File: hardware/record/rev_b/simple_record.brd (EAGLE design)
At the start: 34.9 x 30 mm, 20 parts, among them J1 PJ-035C, J2 SCREW-TERMINAL_2_0.100, J3 SCREW-TERMINAL_2_0.100, J4 SQUALL_HEADER, Q1 MOSFET-NCHANNELSMD, U1 MAX9923T

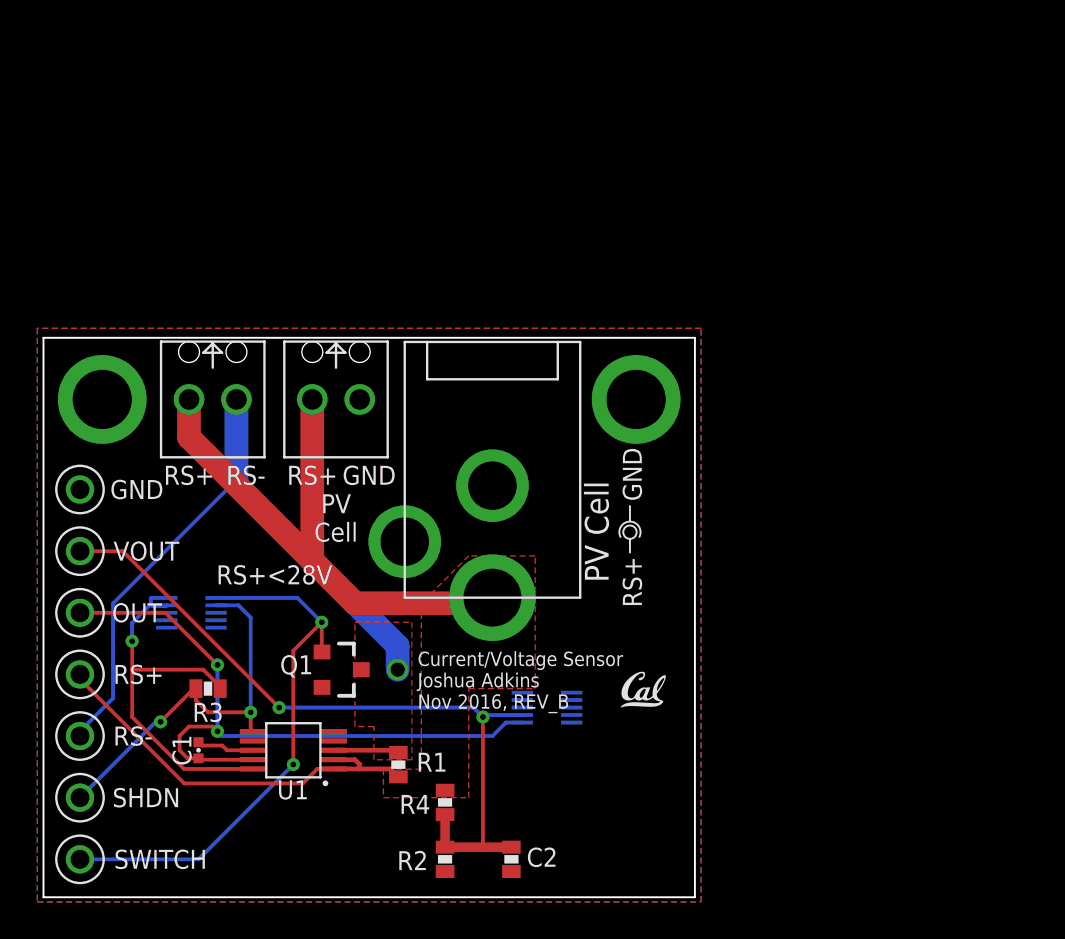
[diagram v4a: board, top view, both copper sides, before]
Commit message: updates
- added second barrel jack
- resized to be same size as logger board
- compressed test points to be 0.1" header friendly
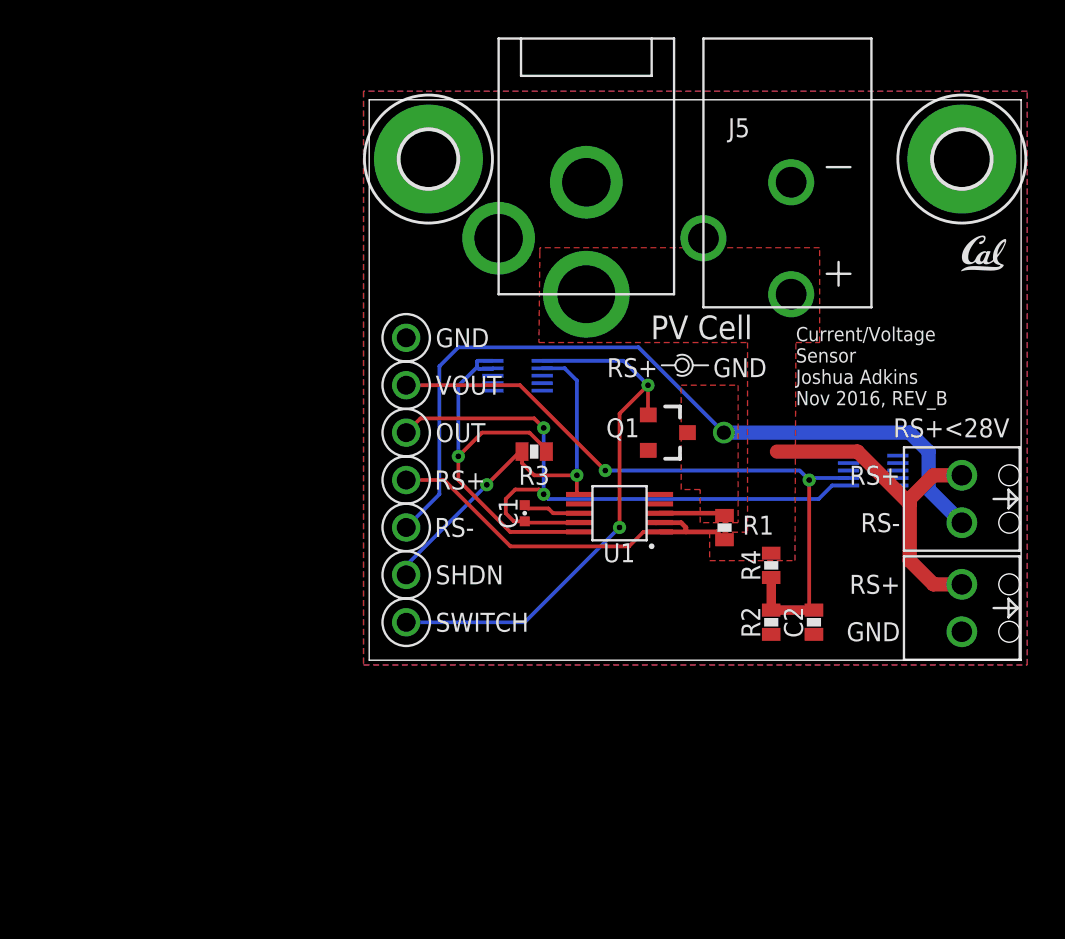
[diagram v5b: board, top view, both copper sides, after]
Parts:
- added H1, H2: MOUNT-PAD-ROUND3.0, holes:3,0-PAD
- added J5: PJ-102AH, connector:PJ-102AH
- moved J3 40.5 mm to (31.8, 8.64), turned to 90 degrees
- moved J2 35.3 mm to (31.8, 2.79), turned to 90 degrees
- moved U$1 29.6 mm to (31.7, 20.8)
- moved C1 21.6 mm to (8.33, 7.87)
- moved J4 21.6 mm to (17.5, 12.7)
- moved Q1 21.6 mm to (16.0, 12.2)
- moved R2 21.6 mm to (21.5, 2.03)
- moved R3 21.6 mm to (8.84, 11.2)
- moved R4 21.6 mm to (21.5, 5.08)
- moved TP3 21.6 mm to (1.98, 2.03)
- moved U1 21.6 mm to (13.4, 7.87)
- moved R1 21.6 mm to (19.0, 7.10)
- moved TP1 21.2 mm to (1.98, 4.57)
- moved TP6 20.7 mm to (1.98, 7.11)
- moved C2 20.6 mm to (23.8, 2.03)
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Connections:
- net GND: now also H1.B3,0, H2.B3,0, J5.2
- net PV+: now also J5.1
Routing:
- net PV+: track 53.1 -> 39.5 mm
- net IN-: track 38.8 -> 46.4 mm
- net VOUT: track 39.7 -> 37.0 mm
- net OUT: track 36.1 -> 35.4 mm
- net SHDN: track 20.7 -> 21.4 mm
- net VCC: track 21.4 -> 21.9 mm

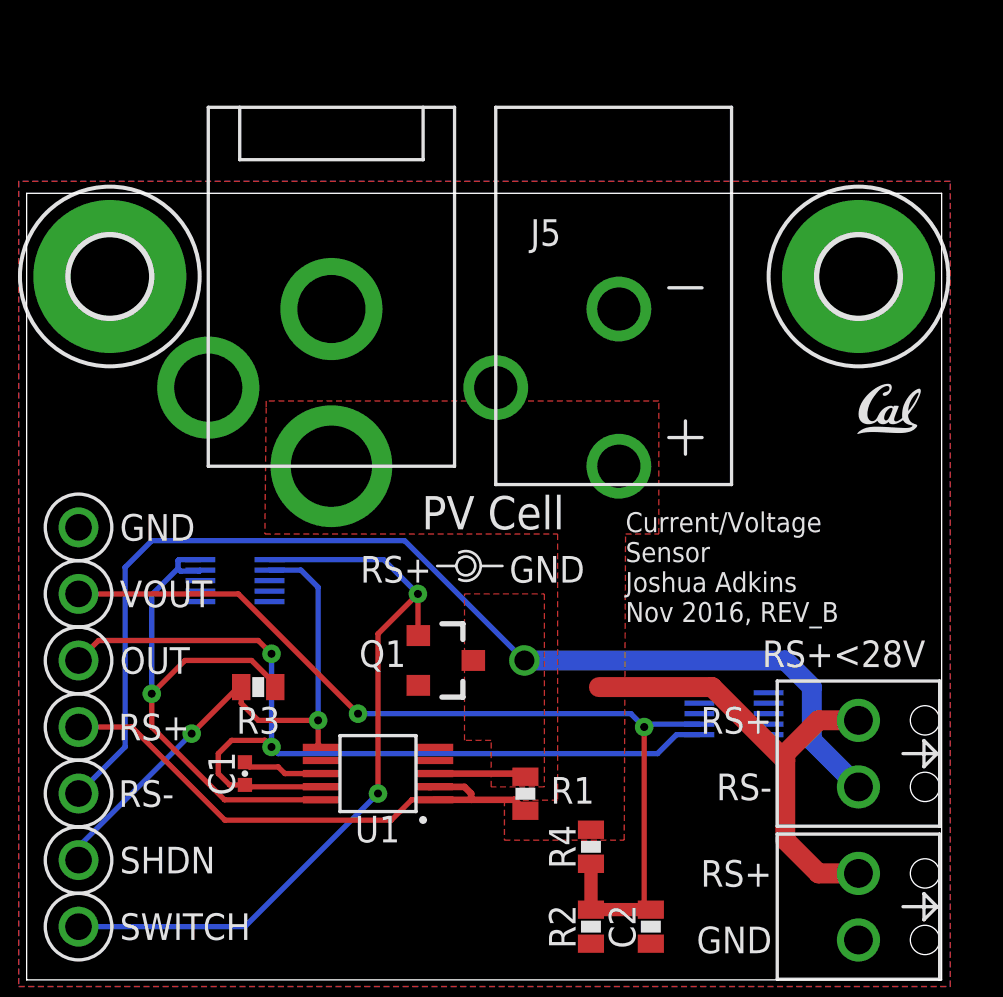
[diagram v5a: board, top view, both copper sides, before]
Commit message: better ground, moved barrel jacks farther out
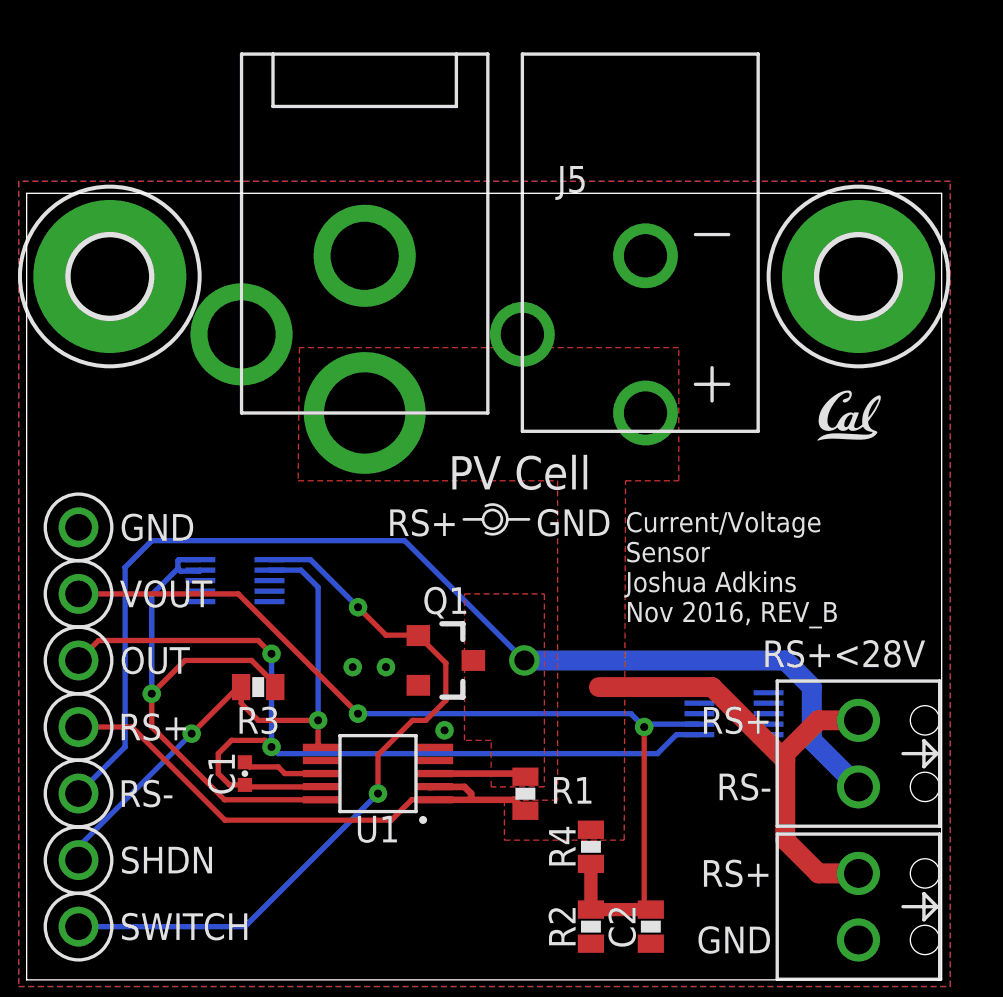
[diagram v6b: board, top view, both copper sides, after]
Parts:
- moved J1 2.40 mm to (12.9, 24.6)
- moved J5 2.27 mm to (23.6, 24.6)
- moved U$1 1.55 mm to (30.2, 20.6)
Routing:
- net CURRENT_SWITCH: track 29.6 -> 28.3 mm
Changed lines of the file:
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@@
 <setting verticaltext="up"/>
 </settings>
-<grid distance="10" unitdist="mil" unit="mil" style="lines" multiple="1" display="yes" altdistance="0.01" altunitdist="inch" altunit="inch"/>
+<grid distance="10" unitdist="mil" unit="mil" style="lines" multiple="1" display="yes" altdistance="1" altunitdist="mil" altunit="mil"/>
 <layers>
 <layer number="1" name="Top" color="4" fill="1" visible="yes" active="yes"/>
@@
 <text x="28.448" y="4.064" size="1.016" layer="25" font="vector" ratio="12" rot="R180" align="center-left">RS+</text>
 <text x="28.448" y="1.524" size="1.016" layer="25" font="vector" ratio="12" rot="R180" align="center-left">GND</text>
-<text x="17.8054" y="17.1958" size="1.27" layer="25" font="vector" ratio="12" align="bottom-center">PV Cell</text>
-<circle x="16.764" y="15.7988" radius="0.359209375" width="0.1016" layer="25"/>
-<wire x1="16.51" y1="16.3068" x2="16.51" y2="15.2908" width="0.1016" layer="25" curve="-233.130102"/>
-<wire x1="17.3482" y1="15.7988" x2="18.161" y2="15.7988" width="0.1016" layer="25"/>
-<wire x1="16.383" y1="15.7988" x2="15.6718" y2="15.7988" width="0.1016" layer="25"/>
-<text x="14.097" y="15.1638" size="1.016" layer="25" font="vector" ratio="12" align="bottom-center">RS+</text>
-<text x="19.8628" y="16.1798" size="1.016" layer="25" font="vector" ratio="12" rot="R180" align="bottom-center">GND</text>
+<text x="18.8214" y="18.7198" size="1.27" layer="25" font="vector" ratio="12" align="bottom-center">PV Cell</text>
+<circle x="17.78" y="17.5768" radius="0.359209375" width="0.1016" layer="25"/>
+<wire x1="17.526" y1="18.0848" x2="17.526" y2="17.0688" width="0.1016" layer="25" curve="-233.130102"/>
+<wire x1="18.3642" y1="17.5768" x2="19.177" y2="17.5768" width="0.1016" layer="25"/>
+<wire x1="17.399" y1="17.5768" x2="16.6878" y2="17.5768" width="0.1016" layer="25"/>
+<text x="15.113" y="16.9418" size="1.016" layer="25" font="vector" ratio="12" align="bottom-center">RS+</text>
+<text x="20.8788" y="17.9578" size="1.016" layer="25" font="vector" ratio="12" rot="R180" align="bottom-center">GND</text>
 <text x="3.556" y="17.272" size="1.016" layer="25" font="vector" ratio="12" align="center-left">GND</text>
 <text x="3.556" y="14.732" size="1.016" layer="25" font="vector" ratio="12" align="center-left">VOUT</text>
@@
 <param name="mdViaViaSameLayer" value="8mil"/>
 <param name="mnLayersViaInSmd" value="2"/>
-<param name="mdCopperDimension" value="20mil"/>
+<param name="mdCopperDimension" value="10mil"/>
 <param name="mdDrill" value="16mil"/>
 <param name="mdSmdStop" value="0mil"/>
@@
 <elements>
 <element name="Q1" library="fets" package="SOT23-3" value="MOSFET-NCHANNELSMD" x="15.9512" y="12.192" smashed="yes" rot="R270">
-<attribute name="NAME" x="13.5852" y="11.944" size="1.016" layer="25" font="vector" ratio="12" align="bottom-center"/>
+<attribute name="NAME" x="16.002" y="13.97" size="1.016" layer="25" font="vector" ratio="12" align="bottom-center"/>
 <attribute name="DIGIKEY" value="DMN3023L-7DICT-ND" x="15.9512" y="12.192" size="1.778" layer="27" rot="R270" display="off"/>
 </element>
@@
 <attribute name="DIGIKEY" value="277-1273-ND" x="31.75" y="8.636" size="1.778" layer="27" font="vector" ratio="12" rot="R90" display="off"/>
 </element>
-<element name="J1" library="connector" package="PJ-035C" value="PJ-035C" x="11.6332" y="22.606" smashed="yes">
-<attribute name="DIGIKEY" value="CP-035C-ND" x="11.6332" y="22.606" size="1.778" layer="27" font="vector" ratio="12" display="off"/>
+<element name="J1" library="connector" package="PJ-035C" value="PJ-035C" x="12.9032" y="24.638" smashed="yes">
+<attribute name="DIGIKEY" value="CP-035C-ND" x="12.9032" y="24.638" size="1.778" layer="27" font="vector" ratio="12" display="off"/>
 </element>
 <element name="U1" library="chips" package="UMAX10" value="MAX9923T" x="13.4112" y="7.874" rot="R90">
@@
 <attribute name="DIGIKEY" value="5001K-ND" x="1.9812" y="12.192" size="1.778" layer="27" font="vector" ratio="12" display="off"/>
 </element>
-<element name="U$1" library="logos" package="UCB_CAL_75MIL" value="UCB_CAL75MIL" x="31.6992" y="20.828"/>
+<element name="U$1" library="logos" package="UCB_CAL_75MIL" value="UCB_CAL75MIL" x="30.1752" y="20.574"/>
 <element name="H1" library="holes" package="3,0-PAD" value="MOUNT-PAD-ROUND3.0" x="31.75" y="26.8478"/>
 <element name="H2" library="holes" package="3,0-PAD" value="MOUNT-PAD-ROUND3.0" x="3.175" y="26.8478"/>
-<element name="J5" library="connector" package="PJ-102AH" value="PJ-102AH" x="22.606" y="22.606" smashed="yes">
-<attribute name="DIGIKEY" value="CP-102AH-ND" x="22.606" y="22.606" size="1.778" layer="27" display="off"/>
-<attribute name="NAME" x="19.812" y="28.018" size="1.016" layer="25" font="vector" ratio="12" align="bottom-center"/>
+<element name="J5" library="connector" package="PJ-102AH" value="PJ-102AH" x="23.622" y="24.638" smashed="yes">
+<attribute name="DIGIKEY" value="CP-102AH-ND" x="23.622" y="24.638" size="1.778" layer="27" display="off"/>
+<attribute name="NAME" x="20.828" y="30.05" size="1.016" layer="25" font="vector" ratio="12" align="bottom-center"/>
 </element>
 </elements>
@@
 <contactref element="H2" pad="B3,0"/>
 <contactref element="J5" pad="2"/>
+<via x="13.716" y="11.938" extent="1-16" drill="0.3048"/>
+<via x="15.9512" y="9.525" extent="1-16" drill="0.3048"/>
+<via x="12.446" y="11.938" extent="1-16" drill="0.3048"/>
 </signal>
 <signal name="PV+">
@@
 <wire x1="16.9672" y1="7.112" x2="16.9672" y2="6.874" width="0.254" layer="1"/>
 <polygon width="0.2032" layer="1" isolate="0.3048" thermals="no">
-<vertex x="24.13" y="22.098"/>
-<vertex x="9.144" y="22.098"/>
-<vertex x="9.144" y="21.844"/>
-<vertex x="9.0932" y="17.018"/>
-<vertex x="20.2692" y="17.018"/>
+<vertex x="24.892" y="24.13"/>
+<vertex x="10.414" y="24.13"/>
+<vertex x="10.3632" y="19.05"/>
+<vertex x="20.2692" y="19.05"/>
 <vertex x="20.2692" y="6.858"/>
 <vertex x="18.2372" y="6.858"/>
 <vertex x="18.2372" y="5.334"/>
 <vertex x="22.8092" y="5.334"/>
-<vertex x="22.86" y="17.018"/>
-<vertex x="24.13" y="17.018"/>
+<vertex x="22.86" y="19.05"/>
+<vertex x="24.892" y="19.05"/>
 </polygon>
 <wire x1="15.5812" y1="6.874" x2="14.6972" y2="6.874" width="0.2032" layer="1"/>
@@
 <contactref element="TP3" pad="TESTPOINT"/>
 <contactref element="J4" pad="A2"/>
-<wire x1="9.2702" y1="16.04" x2="13.6272" y2="16.04" width="0.2032" layer="16"/>
-<wire x1="13.6272" y1="16.04" x2="14.9352" y2="14.732" width="0.2032" layer="16"/>
-<via x="14.9352" y="14.732" extent="1-16" drill="0.3048"/>
-<wire x1="14.9352" y1="14.732" x2="14.9352" y2="13.158" width="0.2032" layer="1"/>
+<via x="12.6492" y="14.224" extent="1-16" drill="0.3048"/>
 <wire x1="14.9352" y1="13.158" x2="14.9512" y2="13.142" width="0.2032" layer="1"/>
 <via x="13.4112" y="7.112" extent="1-16" drill="0.3048"/>
-<wire x1="13.4112" y1="7.112" x2="13.4112" y2="13.208" width="0.2032" layer="1"/>
-<wire x1="13.4112" y1="13.208" x2="14.9352" y2="14.732" width="0.2032" layer="1"/>
 <wire x1="13.4112" y1="7.112" x2="8.3312" y2="2.032" width="0.2032" layer="16"/>
 <wire x1="8.3312" y1="2.032" x2="1.9812" y2="2.032" width="0.2032" layer="16"/>
+<wire x1="13.4112" y1="7.112" x2="13.4112" y2="8.5852" width="0.2032" layer="1"/>
+<wire x1="13.4112" y1="8.5852" x2="14.732" y2="9.906" width="0.2032" layer="1"/>
+<wire x1="14.732" y1="9.906" x2="15.24" y2="9.906" width="0.2032" layer="1"/>
+<wire x1="15.24" y1="9.906" x2="16.002" y2="10.668" width="0.2032" layer="1"/>
+<wire x1="16.002" y1="10.668" x2="16.002" y2="12.0912" width="0.2032" layer="1"/>
+<wire x1="16.002" y1="12.0912" x2="14.9512" y2="13.142" width="0.2032" layer="1"/>
+<wire x1="14.9352" y1="13.158" x2="13.7152" y2="13.158" width="0.2032" layer="1"/>
+<wire x1="13.7152" y1="13.158" x2="12.6492" y2="14.224" width="0.2032" layer="1"/>
+<wire x1="9.2702" y1="16.04" x2="10.8332" y2="16.04" width="0.2032" layer="16"/>
+<wire x1="10.8332" y1="16.04" x2="12.6492" y2="14.224" width="0.2032" layer="16"/>
 </signal>
 <signal name="VCC">
